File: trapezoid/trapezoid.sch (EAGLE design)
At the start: 33 parts, among them U1 MMA8452Q, U4 MCP73831, Y1 CRYSTAL.ABS25

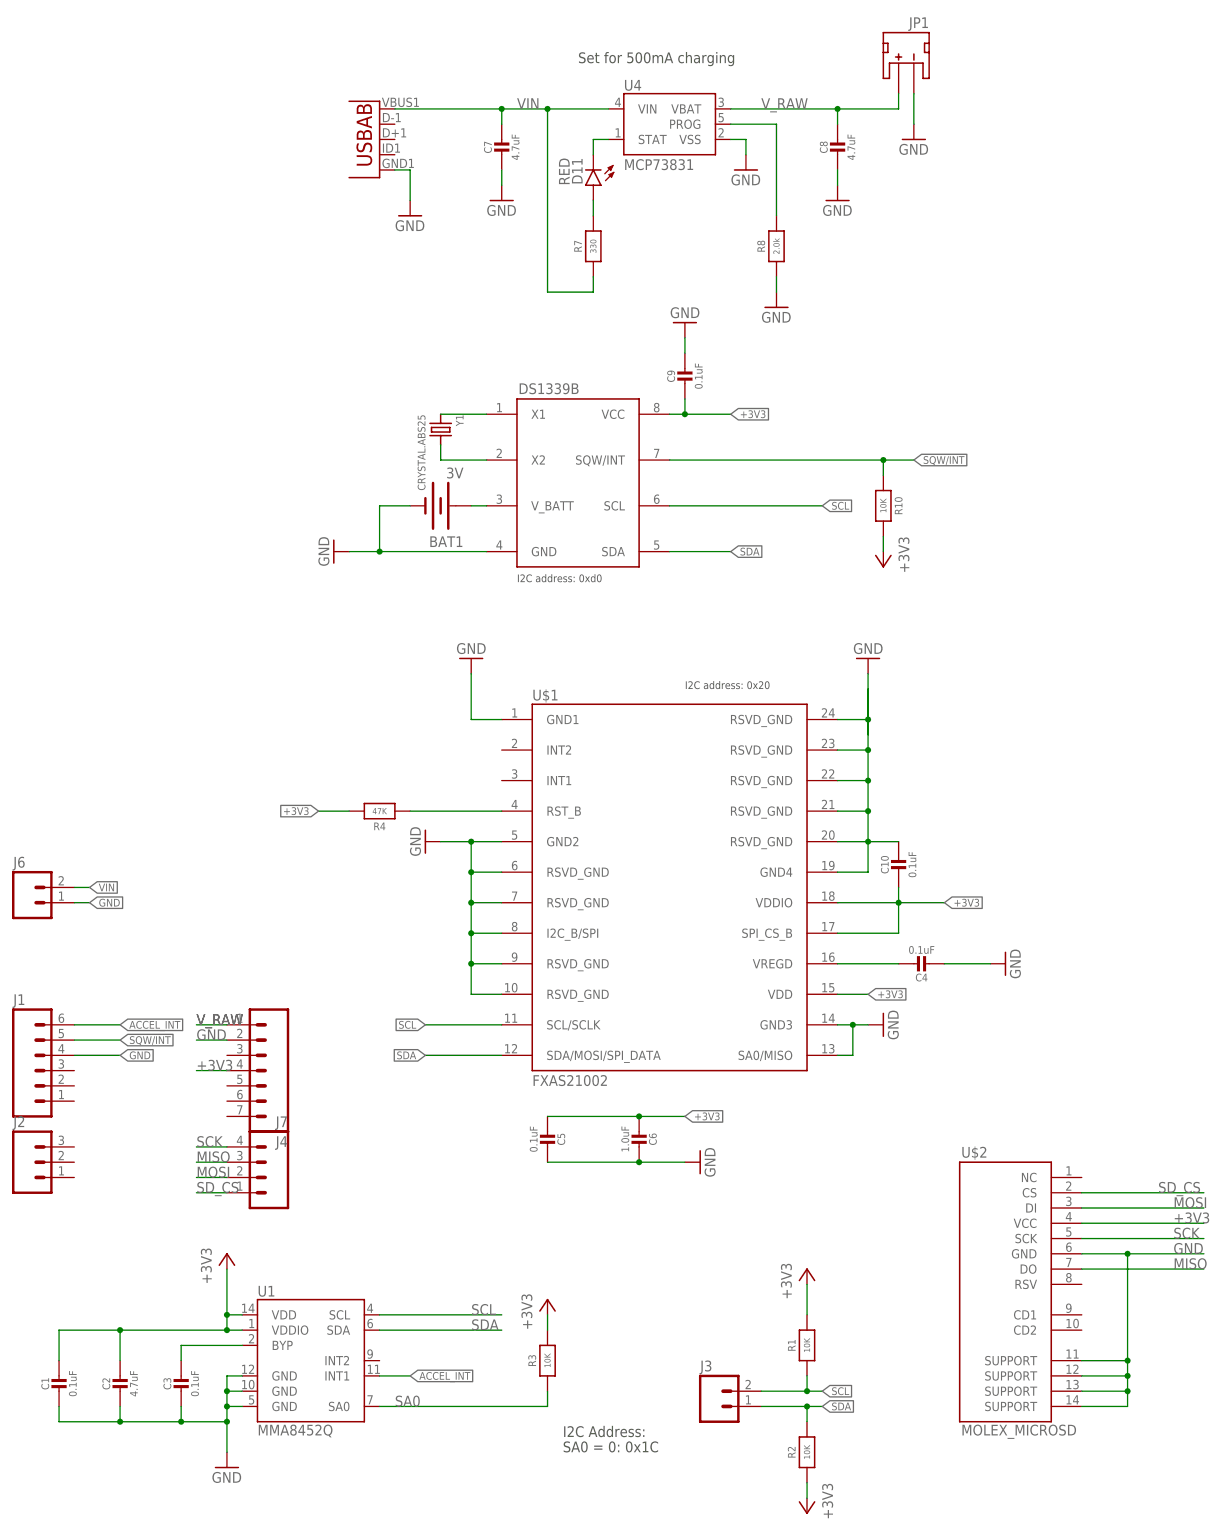
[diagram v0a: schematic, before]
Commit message: removed chargin circuity from schematic
also rerouted battery header pins to connect directly to battery (there is no charger for them to go into any more)
the board layout has not been updated to reflect this change
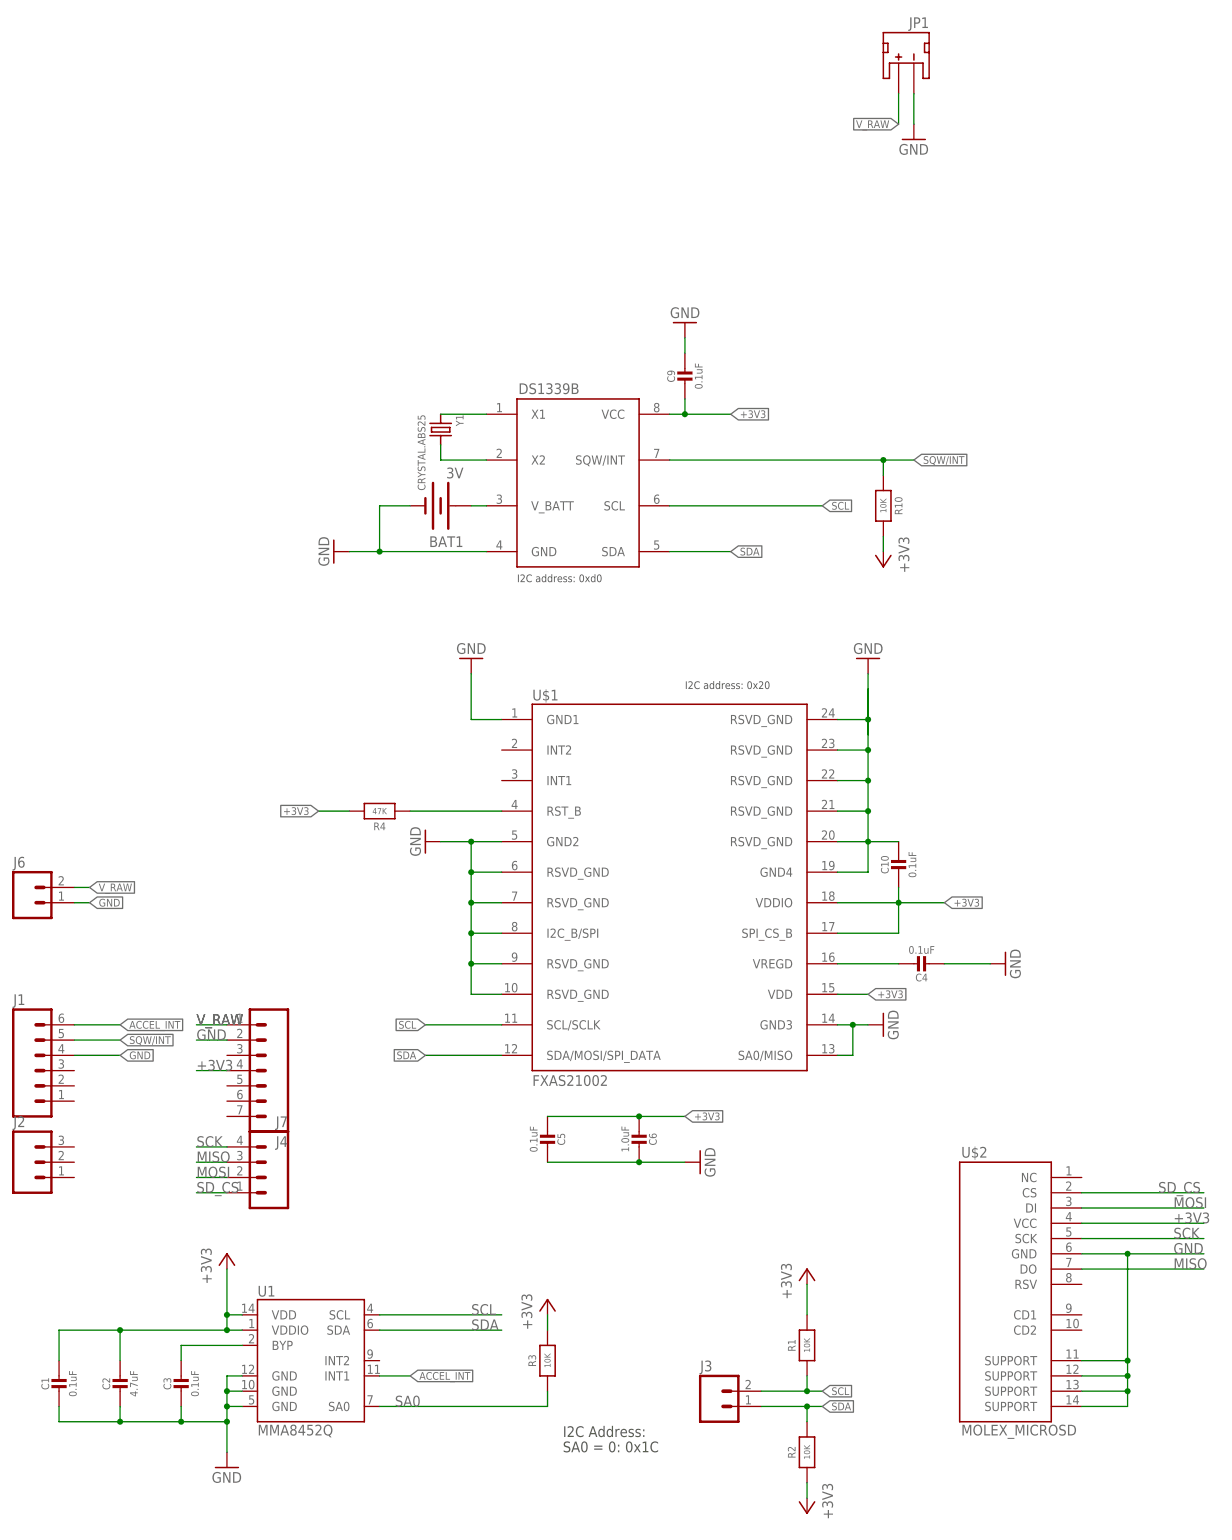
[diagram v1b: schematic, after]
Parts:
- removed C7, C8: 4.7uF, microbuilder:CAP_CERAMIC0805-NOOUTLINE
- removed D11: RED, SparkFun-LED:LED-RED0603
- removed JP9: Micro USB, SparkFun-Connectors:USB-ABCONN-11794
- removed R7: 330, microbuilder:RESISTOR_0805MP
- removed R8: 2.0k, microbuilder:RESISTOR_0805MP
- removed U4: MCP73831, SparkFun-PowerIC:MCP73831
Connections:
- removed net N$1: D11.A, R7.2
- removed net PROG: R8.2, U4.PROG
- removed net STAT: D11.C, U4.STAT
- removed net VIN: C7.1, J6.2, JP9.VBUS, R7.1, U4.VIN
- net GND: no longer C7.2, C8.2, JP9.GND, R8.1, U4.VSS
- net V_RAW: now also J6.2; no longer C8.1, U4.VBAT
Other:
- note removed: "Set for 500mA charging"
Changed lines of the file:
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@@
 <part name="C2" library="microbuilder" deviceset="CAP_CERAMIC" device="0805-NOOUTLINE" value="4.7uF"/>
 <part name="GND4" library="SparkFun" deviceset="GND" device=""/>
-<part name="D11" library="SparkFun-LED" deviceset="LED-RED" device="0603" value="RED"/>
-<part name="GND15" library="SparkFun" deviceset="GND" device=""/>
-<part name="GND14" library="SparkFun" deviceset="GND" device=""/>
-<part name="GND17" library="SparkFun" deviceset="GND" device=""/>
-<part name="GND18" library="SparkFun" deviceset="GND" device=""/>
-<part name="U4" library="SparkFun-PowerIC" deviceset="MCP73831" device=""/>
-<part name="GND19" library="SparkFun" deviceset="GND" device=""/>
-<part name="JP9" library="SparkFun-Connectors" deviceset="USB-AB" device="CONN-11794" value="Micro USB"/>
 <part name="JP1" library="SparkFun-Connectors" deviceset="JST_2MM_MALE" device="" value="JST"/>
-<part name="R7" library="microbuilder" deviceset="RESISTOR" device="_0805MP" value="330"/>
-<part name="R8" library="microbuilder" deviceset="RESISTOR" device="_0805MP" value="2.0k"/>
-<part name="C7" library="microbuilder" deviceset="CAP_CERAMIC" device="0805-NOOUTLINE" value="4.7uF"/>
-<part name="C8" library="microbuilder" deviceset="CAP_CERAMIC" device="0805-NOOUTLINE" value="4.7uF"/>
 <part name="U$3" library="sharkdunio" deviceset="DS1339B" device="DS1339B"/>
 <part name="Y1" library="abracon" deviceset="CRYSTAL" device=".ABS25"/>
@@
 <text x="93.98" y="-25.4" size="1.778" layer="97">I2C Address:</text>
 <text x="93.98" y="-27.94" size="1.778" layer="97">SA0 = 0: 0x1C</text>
-<text x="96.52" y="203.2" size="1.778" layer="97">Set for 500mA charging</text>
 <text x="86.36" y="116.84" size="1.27" layer="97">I2C address: 0xd0</text>
 <text x="114.3" y="99.06" size="1.27" layer="97">I2C address: 0x20</text>
@@
 <instance part="C2" gate="G$1" x="20.32" y="-17.78"/>
 <instance part="GND4" gate="1" x="152.4" y="190.5"/>
-<instance part="D11" gate="G$1" x="99.06" y="182.88" rot="R180"/>
-<instance part="GND15" gate="1" x="68.58" y="177.8"/>
-<instance part="GND14" gate="1" x="139.7" y="180.34"/>
-<instance part="GND17" gate="1" x="83.82" y="180.34"/>
-<instance part="GND18" gate="1" x="124.46" y="185.42"/>
-<instance part="U4" gate="G$1" x="111.76" y="193.04"/>
-<instance part="GND19" gate="1" x="129.54" y="162.56"/>
-<instance part="JP9" gate="G$1" x="60.96" y="190.5" smashed="yes" rot="R180"/>
 <instance part="JP1" gate="G$1" x="152.4" y="203.2" rot="MR0"/>
-<instance part="R7" gate="G$1" x="99.06" y="172.72" rot="R90"/>
-<instance part="R8" gate="G$1" x="129.54" y="172.72" rot="R90"/>
-<instance part="C7" gate="G$1" x="83.82" y="187.96"/>
-<instance part="C8" gate="G$1" x="139.7" y="187.96"/>
 <instance part="U$3" gate="G$1" x="96.52" y="134.62"/>
 <instance part="Y1" gate="G$1" x="73.66" y="142.24" rot="R270"/>
@@
 </segment>
 <segment>
-<wire x1="139.7" y1="182.88" x2="139.7" y2="185.42" width="0.1524" layer="91"/>
-<pinref part="GND14" gate="1" pin="GND"/>
-<pinref part="C8" gate="G$1" pin="2"/>
-</segment>
-<segment>
-<wire x1="83.82" y1="182.88" x2="83.82" y2="185.42" width="0.1524" layer="91"/>
-<pinref part="GND17" gate="1" pin="GND"/>
-<pinref part="C7" gate="G$1" pin="2"/>
-</segment>
-<segment>
-<wire x1="121.92" y1="190.5" x2="124.46" y2="190.5" width="0.1524" layer="91"/>
-<wire x1="124.46" y1="190.5" x2="124.46" y2="187.96" width="0.1524" layer="91"/>
-<pinref part="U4" gate="G$1" pin="VSS"/>
-<pinref part="GND18" gate="1" pin="GND"/>
-</segment>
-<segment>
-<wire x1="129.54" y1="165.1" x2="129.54" y2="167.64" width="0.1524" layer="91"/>
-<pinref part="GND19" gate="1" pin="GND"/>
-<pinref part="R8" gate="G$1" pin="1"/>
-</segment>
-<segment>
-<pinref part="GND15" gate="1" pin="GND"/>
-<pinref part="JP9" gate="G$1" pin="GND"/>
-<wire x1="68.58" y1="180.34" x2="68.58" y2="185.42" width="0.1524" layer="91"/>
-<wire x1="68.58" y1="185.42" x2="66.04" y2="185.42" width="0.1524" layer="91"/>
-</segment>
-<segment>
 <wire x1="152.4" y1="198.12" x2="152.4" y2="193.04" width="0.1524" layer="91"/>
 <pinref part="GND4" gate="1" pin="GND"/>
@@
 </segment>
 <segment>
-<wire x1="139.7" y1="193.04" x2="139.7" y2="195.58" width="0.1524" layer="91"/>
-<wire x1="121.92" y1="195.58" x2="139.7" y2="195.58" width="0.1524" layer="91"/>
-<wire x1="139.7" y1="195.58" x2="149.86" y2="195.58" width="0.1524" layer="91"/>
-<wire x1="149.86" y1="198.12" x2="149.86" y2="195.58" width="0.1524" layer="91"/>
-<junction x="139.7" y="195.58"/>
-<label x="127" y="195.58" size="1.778" layer="95"/>
-<pinref part="U4" gate="G$1" pin="VBAT"/>
 <pinref part="JP1" gate="G$1" pin="+"/>
-<pinref part="C8" gate="G$1" pin="1"/>
+<label x="149.86" y="193.04" size="1.27" layer="95" rot="R180" xref="yes"/>
+<wire x1="149.86" y1="198.12" x2="149.86" y2="193.04" width="0.1524" layer="91"/>
+</segment>
+<segment>
+<pinref part="J6" gate="G$1" pin="2"/>
+<wire x1="12.7" y1="66.04" x2="15.24" y2="66.04" width="0.1524" layer="91"/>
+<label x="15.24" y="66.04" size="1.27" layer="95" xref="yes"/>
 </segment>
 </net>
@@
 </segment>
 </net>
-<net name="N$1" class="0">
-<segment>
-<wire x1="99.06" y1="177.8" x2="99.06" y2="180.34" width="0.1524" layer="91"/>
-<pinref part="D11" gate="G$1" pin="A"/>
-<pinref part="R7" gate="G$1" pin="2"/>
-</segment>
-</net>
-<net name="PROG" class="0">
-<segment>
-<wire x1="121.92" y1="193.04" x2="129.54" y2="193.04" width="0.1524" layer="91"/>
-<wire x1="129.54" y1="193.04" x2="129.54" y2="177.8" width="0.1524" layer="91"/>
-<pinref part="U4" gate="G$1" pin="PROG"/>
-<pinref part="R8" gate="G$1" pin="2"/>
-</segment>
-</net>
-<net name="STAT" class="0">
-<segment>
-<wire x1="99.06" y1="190.5" x2="99.06" y2="187.96" width="0.1524" layer="91"/>
-<wire x1="101.6" y1="190.5" x2="99.06" y2="190.5" width="0.1524" layer="91"/>
-<pinref part="D11" gate="G$1" pin="C"/>
-<pinref part="U4" gate="G$1" pin="STAT"/>
-</segment>
-</net>
-<net name="VIN" class="0">
-<segment>
-<wire x1="99.06" y1="167.64" x2="99.06" y2="165.1" width="0.1524" layer="91"/>
-<wire x1="83.82" y1="193.04" x2="83.82" y2="195.58" width="0.1524" layer="91"/>
-<wire x1="83.82" y1="195.58" x2="91.44" y2="195.58" width="0.1524" layer="91"/>
-<wire x1="91.44" y1="195.58" x2="101.6" y2="195.58" width="0.1524" layer="91"/>
-<wire x1="99.06" y1="165.1" x2="91.44" y2="165.1" width="0.1524" layer="91"/>
-<wire x1="91.44" y1="165.1" x2="91.44" y2="195.58" width="0.1524" layer="91"/>
-<wire x1="66.04" y1="195.58" x2="83.82" y2="195.58" width="0.1524" layer="91"/>
-<junction x="83.82" y="195.58"/>
-<junction x="91.44" y="195.58"/>
-<label x="86.36" y="195.58" size="1.778" layer="95"/>
-<pinref part="U4" gate="G$1" pin="VIN"/>
-<pinref part="JP9" gate="G$1" pin="VBUS"/>
-<pinref part="R7" gate="G$1" pin="1"/>
-<pinref part="C7" gate="G$1" pin="1"/>
-</segment>
-<segment>
-<pinref part="J6" gate="G$1" pin="2"/>
-<wire x1="12.7" y1="66.04" x2="15.24" y2="66.04" width="0.1524" layer="91"/>
-<label x="15.24" y="66.04" size="1.27" layer="95" xref="yes"/>
-</segment>
-</net>

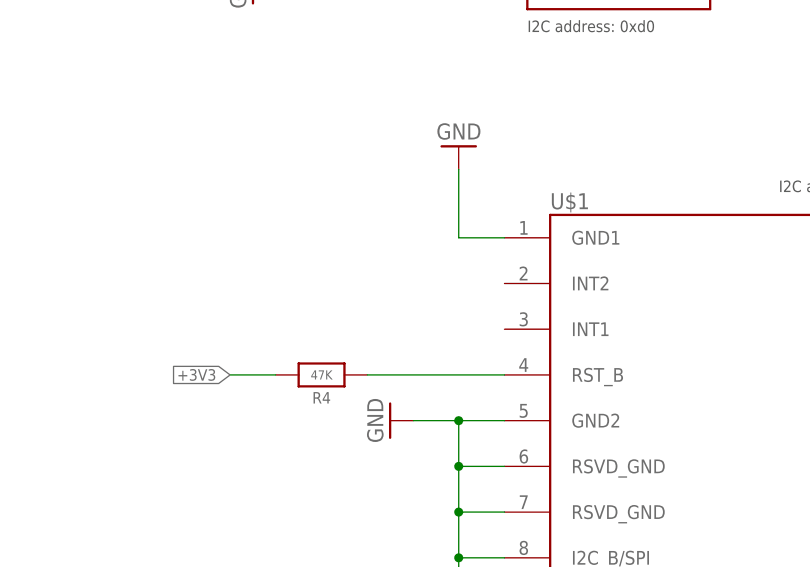
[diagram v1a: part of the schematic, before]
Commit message: connect gyro int2 to pin3
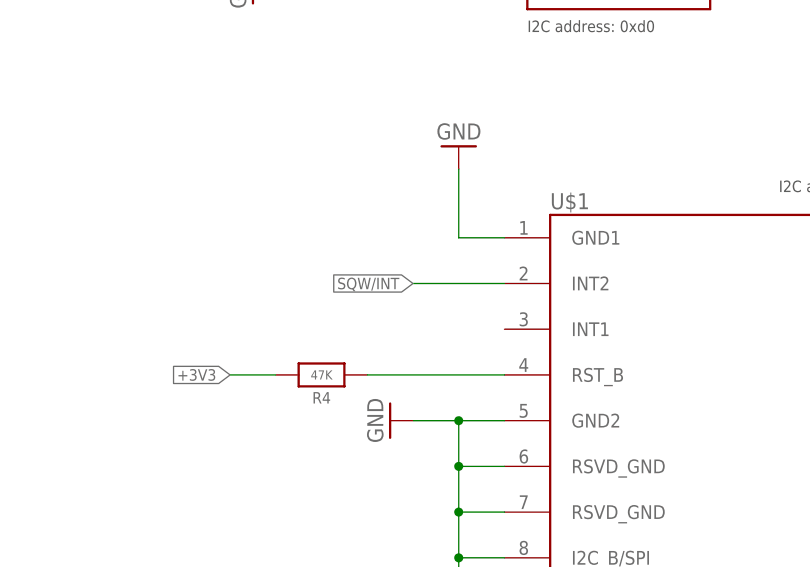
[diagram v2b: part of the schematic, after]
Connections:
- net SQW/INT: now also U$1.INT2
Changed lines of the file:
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@@
 <pinref part="J1" gate="G$1" pin="5"/>
+</segment>
+<segment>
+<pinref part="U$1" gate="G$1" pin="INT2"/>
+<wire x1="83.82" y1="88.9" x2="73.66" y2="88.9" width="0.1524" layer="91"/>
+<label x="73.66" y="88.9" size="1.27" layer="95" rot="R180" xref="yes"/>
 </segment>
 </net>
